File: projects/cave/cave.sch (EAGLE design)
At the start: 111 parts, among them U1 IRLML6344TRPBF, U10 IRLML6344TRPBF, U11 IRLML6344TRPBF, U12 IRLML6344TRPBF, U2 TLC555CDR, U3 IRLML6344TRPBF, U4 IRLML6344TRPBF, U5 IRLML6344TRPBF, U6 IRLML6344TRPBF, U7 TPS54625, U9 IRLML6344TRPBF

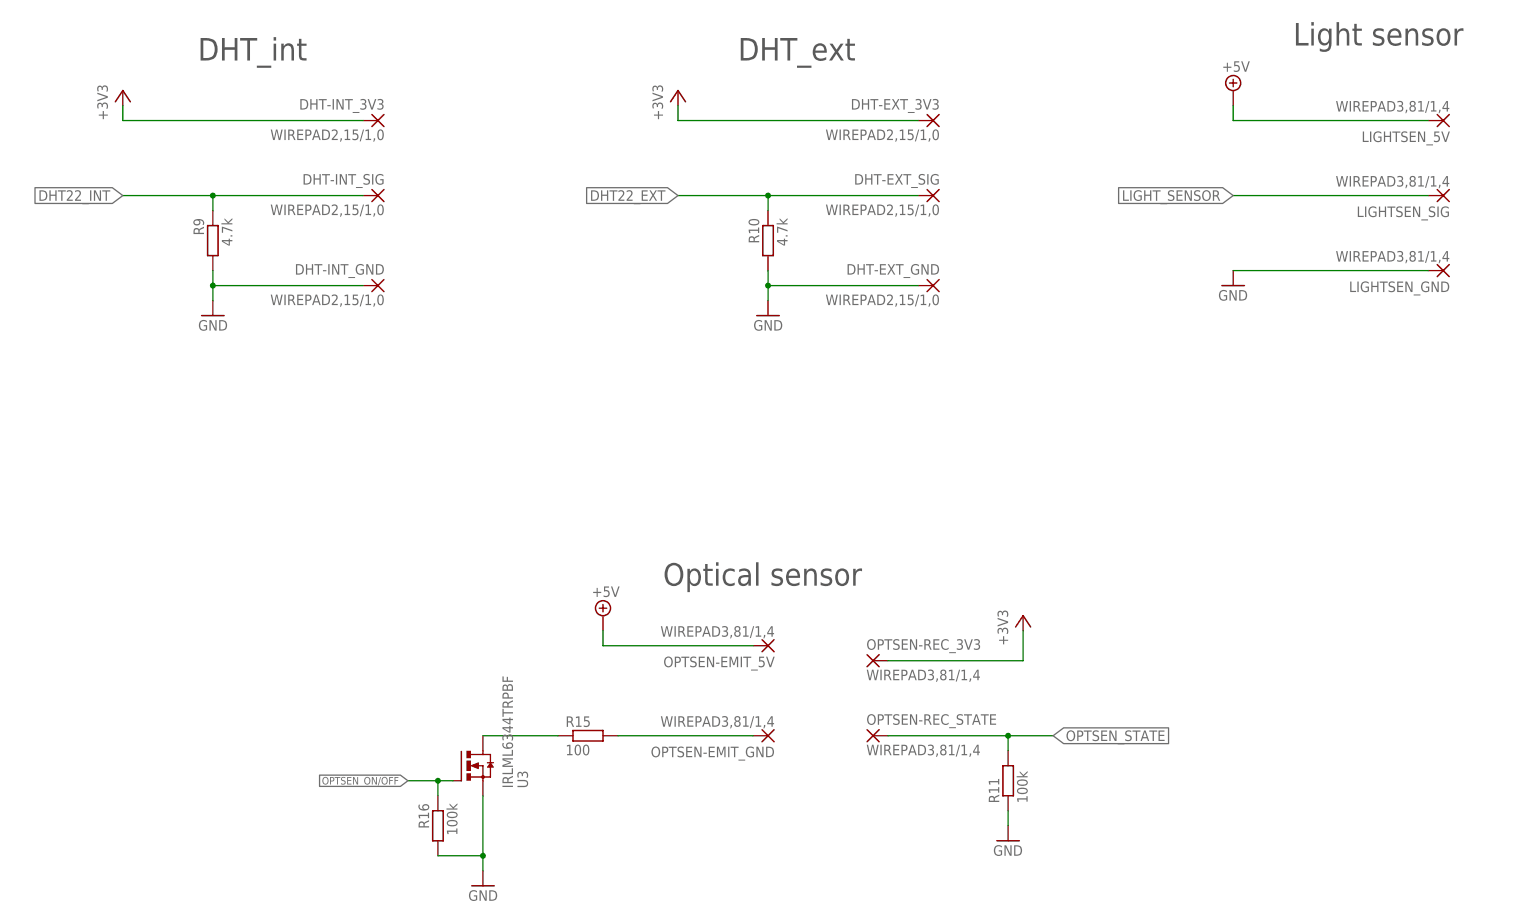
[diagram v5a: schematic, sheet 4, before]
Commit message: Routing IO wirepads to 40-pin header.
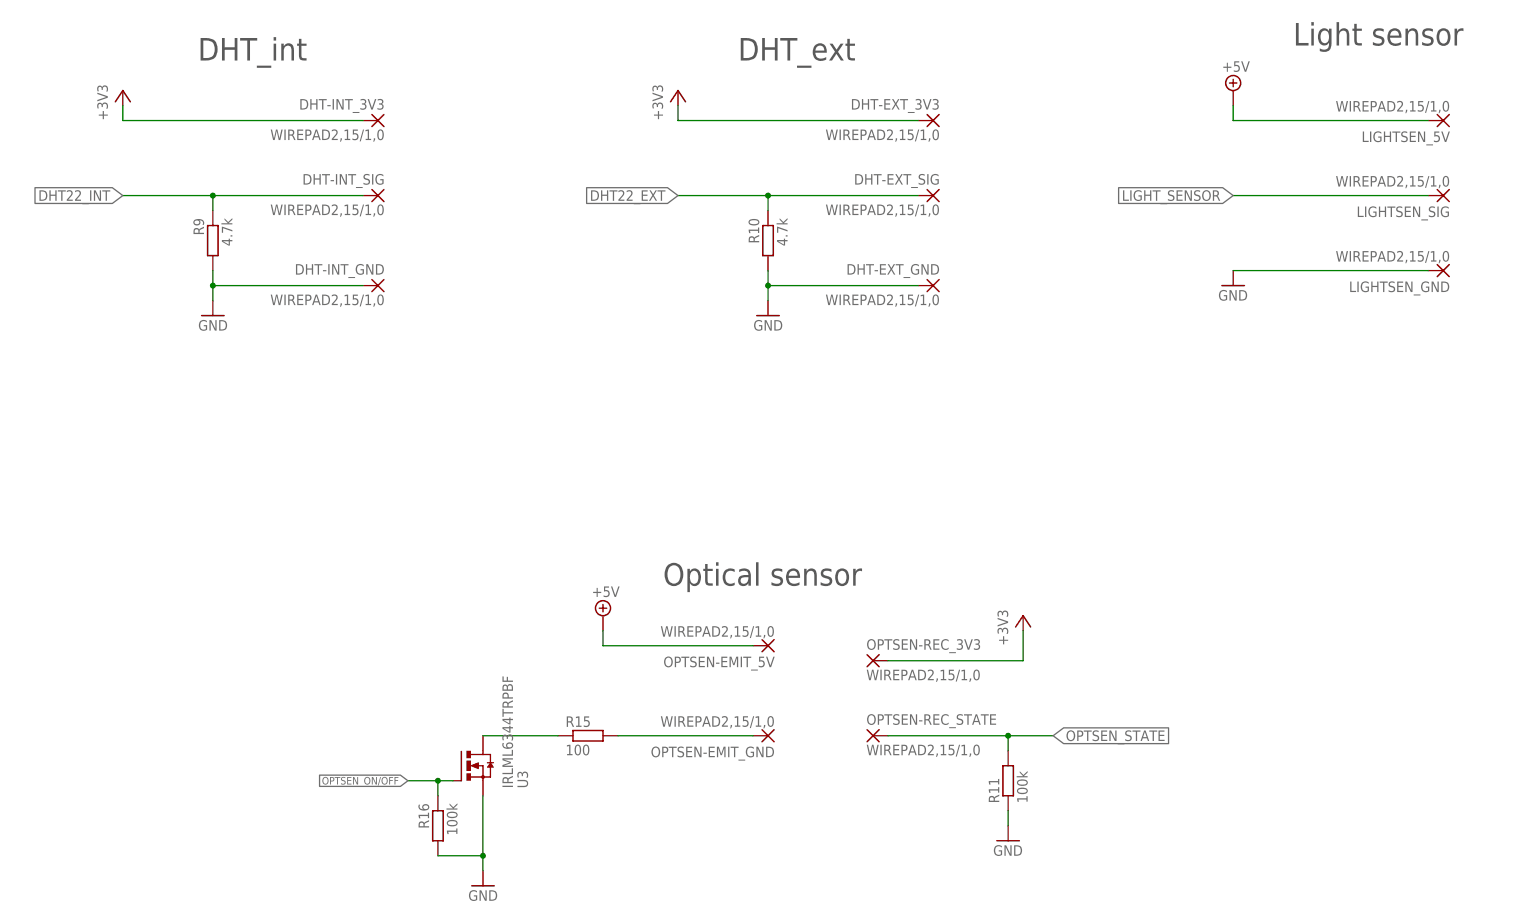
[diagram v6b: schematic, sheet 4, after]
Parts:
- BUZZER+, BUZZER-, DEHUM_SWITCH+, DEHUM_SWITCH_GND, FAN_SWITCH+, FAN_SWITCH_GND, HEAT_SWITCH+, HEAT_SWITCH_GND, LIGHTSEN_5V, LIGHTSEN_GND, LIGHTSEN_SIG, OPTSEN-EMIT_5V, OPTSEN-EMIT_GND, OPTSEN-REC_3V3, OPTSEN-REC_STATE, SERVO_5V, SERVO_GND, SERVO_PWM: value WIREPAD3,81/1,4 -> WIREPAD2,15/1,0; device wirepad:WIREPAD3,81/1,4 -> wirepad:WIREPAD2,15/1,0
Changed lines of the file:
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@@
 <part name="R2" library="rcl" deviceset="R-EU_" device="R0603" value="100k"/>
 <part name="R3" library="rcl" deviceset="R-EU_" device="R0603" value="37.4k"/>
-<part name="SERVO_5V" library="wirepad" deviceset="WIREPAD" device="3,81/1,4"/>
-<part name="SERVO_PWM" library="wirepad" deviceset="WIREPAD" device="3,81/1,4"/>
-<part name="SERVO_GND" library="wirepad" deviceset="WIREPAD" device="3,81/1,4"/>
+<part name="SERVO_5V" library="wirepad" deviceset="WIREPAD" device="2,15/1,0" value="WIREPAD2,15/1,0"/>
+<part name="SERVO_PWM" library="wirepad" deviceset="WIREPAD" device="2,15/1,0" value="WIREPAD2,15/1,0"/>
+<part name="SERVO_GND" library="wirepad" deviceset="WIREPAD" device="2,15/1,0" value="WIREPAD2,15/1,0"/>
 <part name="GND1" library="supply1" deviceset="GND" device=""/>
 <part name="R1" library="rcl" deviceset="R-EU_" device="R0603" value="100k"/>
@@
 <part name="DHT-EXT_3V3" library="wirepad" deviceset="WIREPAD" device="2,15/1,0" value="WIREPAD2,15/1,0"/>
 <part name="R10" library="rcl" deviceset="R-EU_" device="R0603" value="4.7k"/>
-<part name="OPTSEN-EMIT_GND" library="wirepad" deviceset="WIREPAD" device="3,81/1,4"/>
-<part name="OPTSEN-EMIT_5V" library="wirepad" deviceset="WIREPAD" device="3,81/1,4"/>
-<part name="OPTSEN-REC_STATE" library="wirepad" deviceset="WIREPAD" device="3,81/1,4"/>
-<part name="OPTSEN-REC_3V3" library="wirepad" deviceset="WIREPAD" device="3,81/1,4"/>
+<part name="OPTSEN-EMIT_GND" library="wirepad" deviceset="WIREPAD" device="2,15/1,0" value="WIREPAD2,15/1,0"/>
+<part name="OPTSEN-EMIT_5V" library="wirepad" deviceset="WIREPAD" device="2,15/1,0" value="WIREPAD2,15/1,0"/>
+<part name="OPTSEN-REC_STATE" library="wirepad" deviceset="WIREPAD" device="2,15/1,0" value="WIREPAD2,15/1,0"/>
+<part name="OPTSEN-REC_3V3" library="wirepad" deviceset="WIREPAD" device="2,15/1,0" value="WIREPAD2,15/1,0"/>
 <part name="R11" library="rcl" deviceset="R-EU_" device="R0603" value="100k"/>
 <part name="GND3" library="supply1" deviceset="GND" device=""/>
@@
 <part name="R16" library="rcl" deviceset="R-EU_" device="R0603" value="100k"/>
 <part name="GND7" library="supply1" deviceset="GND" device=""/>
-<part name="LIGHTSEN_5V" library="wirepad" deviceset="WIREPAD" device="3,81/1,4"/>
-<part name="LIGHTSEN_SIG" library="wirepad" deviceset="WIREPAD" device="3,81/1,4"/>
-<part name="LIGHTSEN_GND" library="wirepad" deviceset="WIREPAD" device="3,81/1,4"/>
+<part name="LIGHTSEN_5V" library="wirepad" deviceset="WIREPAD" device="2,15/1,0" value="WIREPAD2,15/1,0"/>
+<part name="LIGHTSEN_SIG" library="wirepad" deviceset="WIREPAD" device="2,15/1,0" value="WIREPAD2,15/1,0"/>
+<part name="LIGHTSEN_GND" library="wirepad" deviceset="WIREPAD" device="2,15/1,0" value="WIREPAD2,15/1,0"/>
 <part name="GND8" library="supply1" deviceset="GND" device=""/>
 <part name="T1" library="transistor" deviceset="*-NPN-" device="SOT23-BEC" technology="MMBT2369LT1"/>
@@
 <part name="GND11" library="supply1" deviceset="GND" device=""/>
 <part name="R23" library="rcl" deviceset="R-EU_" device="R0603" value="10k"/>
-<part name="HEAT_SWITCH_GND" library="wirepad" deviceset="WIREPAD" device="3,81/1,4"/>
+<part name="HEAT_SWITCH_GND" library="wirepad" deviceset="WIREPAD" device="2,15/1,0" value="WIREPAD2,15/1,0"/>
 <part name="R24" library="rcl" deviceset="R-EU_" device="R0603" value="250"/>
 <part name="U4" library="transistor-power" deviceset="IRLML6344TRPBF" device=""/>
@@
 <part name="R38" library="rcl" deviceset="R-EU_" device="R0603" value="250"/>
 <part name="FRAME1" library="frames" deviceset="FRAME_A_L" device=""/>
-<part name="BUZZER+" library="wirepad" deviceset="WIREPAD" device="3,81/1,4"/>
-<part name="BUZZER-" library="wirepad" deviceset="WIREPAD" device="3,81/1,4"/>
+<part name="BUZZER+" library="wirepad" deviceset="WIREPAD" device="2,15/1,0" value="WIREPAD2,15/1,0"/>
+<part name="BUZZER-" library="wirepad" deviceset="WIREPAD" device="2,15/1,0" value="WIREPAD2,15/1,0"/>
 <part name="U10" library="transistor-power" deviceset="IRLML6344TRPBF" device=""/>
 <part name="R39" library="rcl" deviceset="R-EU_" device="R0603" value="100k"/>
@@
 <part name="FRAME5" library="frames" deviceset="FRAME_A_L" device=""/>
 <part name="GND21" library="supply1" deviceset="GND" device=""/>
-<part name="DEHUM_SWITCH_GND" library="wirepad" deviceset="WIREPAD" device="3,81/1,4"/>
+<part name="DEHUM_SWITCH_GND" library="wirepad" deviceset="WIREPAD" device="2,15/1,0" value="WIREPAD2,15/1,0"/>
 <part name="R40" library="rcl" deviceset="R-EU_" device="R0603" value="250"/>
 <part name="U11" library="transistor-power" deviceset="IRLML6344TRPBF" device=""/>
@@
 <part name="C1" library="rcl" deviceset="C-EU" device="C0805" value="10uF/25V"/>
 <part name="GND12" library="supply1" deviceset="GND" device=""/>
-<part name="FAN_SWITCH_GND" library="wirepad" deviceset="WIREPAD" device="3,81/1,4"/>
-<part name="FAN_SWITCH+" library="wirepad" deviceset="WIREPAD" device="3,81/1,4"/>
+<part name="FAN_SWITCH_GND" library="wirepad" deviceset="WIREPAD" device="2,15/1,0" value="WIREPAD2,15/1,0"/>
+<part name="FAN_SWITCH+" library="wirepad" deviceset="WIREPAD" device="2,15/1,0" value="WIREPAD2,15/1,0"/>
 <part name="R28" library="rcl" deviceset="R-EU_" device="R0603" value="250"/>
 <part name="U6" library="transistor-power" deviceset="IRLML6344TRPBF" device=""/>
@@
 <part name="F-12V" library="rcl" deviceset="R-EU_" device="R0805" value="0"/>
 <part name="F-5V" library="rcl" deviceset="R-EU_" device="R0805" value="0"/>
-<part name="HEAT_SWITCH+" library="wirepad" deviceset="WIREPAD" device="3,81/1,4"/>
+<part name="HEAT_SWITCH+" library="wirepad" deviceset="WIREPAD" device="2,15/1,0" value="WIREPAD2,15/1,0"/>
 <part name="H-12V" library="rcl" deviceset="R-EU_" device="R0805" value="0"/>
 <part name="H-5V" library="rcl" deviceset="R-EU_" device="R0805" value="0"/>
-<part name="DEHUM_SWITCH+" library="wirepad" deviceset="WIREPAD" device="3,81/1,4"/>
+<part name="DEHUM_SWITCH+" library="wirepad" deviceset="WIREPAD" device="2,15/1,0" value="WIREPAD2,15/1,0"/>
 <part name="D-12V" library="rcl" deviceset="R-EU_" device="R0805" value="0"/>
 <part name="D-5V" library="rcl" deviceset="R-EU_" device="R0805" value="0"/>

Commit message: Routing in progress...
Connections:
- removed net SPI_CLK: X2.9
- net SPI_SCLK: now also X2.9
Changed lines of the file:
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@@
 <grid distance="0.1" unitdist="inch" unit="inch" style="lines" multiple="1" display="no" altdistance="0.01" altunitdist="inch" altunit="inch"/>
 <layers>
-<layer number="1" name="Top" color="4" fill="1" visible="yes" active="no"/>
-<layer number="2" name="Route2" color="1" fill="3" visible="yes" active="no"/>
-<layer number="3" name="Route3" color="4" fill="3" visible="yes" active="no"/>
-<layer number="14" name="Route14" color="1" fill="6" visible="yes" active="no"/>
-<layer number="15" name="Route15" color="4" fill="6" visible="yes" active="no"/>
-<layer number="16" name="Bottom" color="1" fill="1" visible="yes" active="no"/>
-<layer number="17" name="Pads" color="2" fill="1" visible="yes" active="no"/>
-<layer number="18" name="Vias" color="2" fill="1" visible="yes" active="no"/>
-<layer number="19" name="Unrouted" color="6" fill="1" visible="yes" active="no"/>
-<layer number="20" name="Dimension" color="15" fill="1" visible="yes" active="no"/>
-<layer number="21" name="tPlace" color="7" fill="1" visible="yes" active="no"/>
-<layer number="22" name="bPlace" color="7" fill="1" visible="yes" active="no"/>
-<layer number="23" name="tOrigins" color="15" fill="1" visible="yes" active="no"/>
-<layer number="24" name="bOrigins" color="15" fill="1" visible="yes" active="no"/>
-<layer number="25" name="tNames" color="7" fill="1" visible="yes" active="no"/>
-<layer number="26" name="bNames" color="7" fill="1" visible="yes" active="no"/>
-<layer number="27" name="tValues" color="7" fill="1" visible="yes" active="no"/>
-<layer number="28" name="bValues" color="7" fill="1" visible="yes" active="no"/>
+<layer number="1" name="Top" color="4" fill="1" visible="no" active="no"/>
+<layer number="2" name="Route2" color="1" fill="3" visible="no" active="no"/>
+<layer number="3" name="Route3" color="4" fill="3" visible="no" active="no"/>
+<layer number="14" name="Route14" color="1" fill="6" visible="no" active="no"/>
+<layer number="15" name="Route15" color="4" fill="6" visible="no" active="no"/>
+<layer number="16" name="Bottom" color="1" fill="1" visible="no" active="no"/>
+<layer number="17" name="Pads" color="2" fill="1" visible="no" active="no"/>
+<layer number="18" name="Vias" color="2" fill="1" visible="no" active="no"/>
+<layer number="19" name="Unrouted" color="6" fill="1" visible="no" active="no"/>
+<layer number="20" name="Dimension" color="15" fill="1" visible="no" active="no"/>
+<layer number="21" name="tPlace" color="7" fill="1" visible="no" active="no"/>
+<layer number="22" name="bPlace" color="7" fill="1" visible="no" active="no"/>
+<layer number="23" name="tOrigins" color="15" fill="1" visible="no" active="no"/>
+<layer number="24" name="bOrigins" color="15" fill="1" visible="no" active="no"/>
+<layer number="25" name="tNames" color="7" fill="1" visible="no" active="no"/>
+<layer number="26" name="bNames" color="7" fill="1" visible="no" active="no"/>
+<layer number="27" name="tValues" color="7" fill="1" visible="no" active="no"/>
+<layer number="28" name="bValues" color="7" fill="1" visible="no" active="no"/>
 <layer number="29" name="tStop" color="7" fill="3" visible="no" active="no"/>
 <layer number="30" name="bStop" color="7" fill="6" visible="no" active="no"/>
@@
 <layer number="35" name="tGlue" color="7" fill="4" visible="no" active="no"/>
 <layer number="36" name="bGlue" color="7" fill="5" visible="no" active="no"/>
-<layer number="37" name="tTest" color="7" fill="1" visible="yes" active="no"/>
-<layer number="38" name="bTest" color="7" fill="1" visible="yes" active="no"/>
+<layer number="37" name="tTest" color="7" fill="1" visible="no" active="no"/>
+<layer number="38" name="bTest" color="7" fill="1" visible="no" active="no"/>
 <layer number="39" name="tKeepout" color="4" fill="11" visible="no" active="no"/>
 <layer number="40" name="bKeepout" color="1" fill="11" visible="no" active="no"/>
@@
 <layer number="44" name="Drills" color="7" fill="1" visible="no" active="no"/>
 <layer number="45" name="Holes" color="7" fill="1" visible="no" active="no"/>
-<layer number="46" name="Milling" color="3" fill="1" visible="yes" active="no"/>
-<layer number="47" name="Measures" color="7" fill="1" visible="yes" active="no"/>
-<layer number="48" name="Document" color="7" fill="1" visible="yes" active="no"/>
-<layer number="49" name="Reference" color="7" fill="1" visible="yes" active="no"/>
-<layer number="50" name="dxf" color="7" fill="1" visible="yes" active="no"/>
-<layer number="51" name="tDocu" color="7" fill="1" visible="yes" active="no"/>
-<layer number="52" name="bDocu" color="7" fill="1" visible="yes" active="no"/>
-<layer number="53" name="tGND_GNDA" color="7" fill="9" visible="yes" active="no"/>
-<layer number="54" name="bGND_GNDA" color="1" fill="9" visible="yes" active="no"/>
-<layer number="56" name="wert" color="7" fill="1" visible="yes" active="no"/>
-<layer number="59" name="Invisible" color="7" fill="1" visible="yes" active="no"/>
-<layer number="61" name="stand" color="7" fill="1" visible="yes" active="no"/>
+<layer number="46" name="Milling" color="3" fill="1" visible="no" active="no"/>
+<layer number="47" name="Measures" color="7" fill="1" visible="no" active="no"/>
+<layer number="48" name="Document" color="7" fill="1" visible="no" active="no"/>
+<layer number="49" name="Reference" color="7" fill="1" visible="no" active="no"/>
+<layer number="50" name="dxf" color="7" fill="1" visible="no" active="no"/>
+<layer number="51" name="tDocu" color="7" fill="1" visible="no" active="no"/>
+<layer number="52" name="bDocu" color="7" fill="1" visible="no" active="no"/>
+<layer number="53" name="tGND_GNDA" color="7" fill="9" visible="no" active="no"/>
+<layer number="54" name="bGND_GNDA" color="1" fill="9" visible="no" active="no"/>
+<layer number="56" name="wert" color="7" fill="1" visible="no" active="no"/>
+<layer number="59" name="Invisible" color="7" fill="1" visible="no" active="no"/>
+<layer number="61" name="stand" color="7" fill="1" visible="no" active="no"/>
 <layer number="90" name="Modules" color="5" fill="1" visible="yes" active="yes"/>
 <layer number="91" name="Nets" color="2" fill="1" visible="yes" active="yes"/>
@@
 <label x="137.16" y="55.88" size="1.016" layer="95" rot="R180" xref="yes"/>
 </segment>
+<segment>
+<pinref part="X2" gate="G$1" pin="9"/>
+<wire x1="241.3" y1="2.54" x2="243.84" y2="2.54" width="0.1524" layer="91"/>
+<label x="243.84" y="2.54" size="1.27" layer="95" xref="yes"/>
+</segment>
 </net>
 <net name="EEPROM_SD" class="0">
@@
 </segment>
 </net>
-<net name="SPI_CLK" class="0">
-<segment>
-<pinref part="X2" gate="G$1" pin="9"/>
-<wire x1="241.3" y1="2.54" x2="243.84" y2="2.54" width="0.1524" layer="91"/>
-<label x="243.84" y="2.54" size="1.27" layer="95" xref="yes"/>
-</segment>
-</net>
